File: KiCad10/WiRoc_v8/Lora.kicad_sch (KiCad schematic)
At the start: 16 parts, among them J1 TC2050, J11 Conn_01x05, J9 Conn_Coaxial, SW2 SW_SPST, U20 SY6280, U8 RAK3172-xx-43-SM-xI

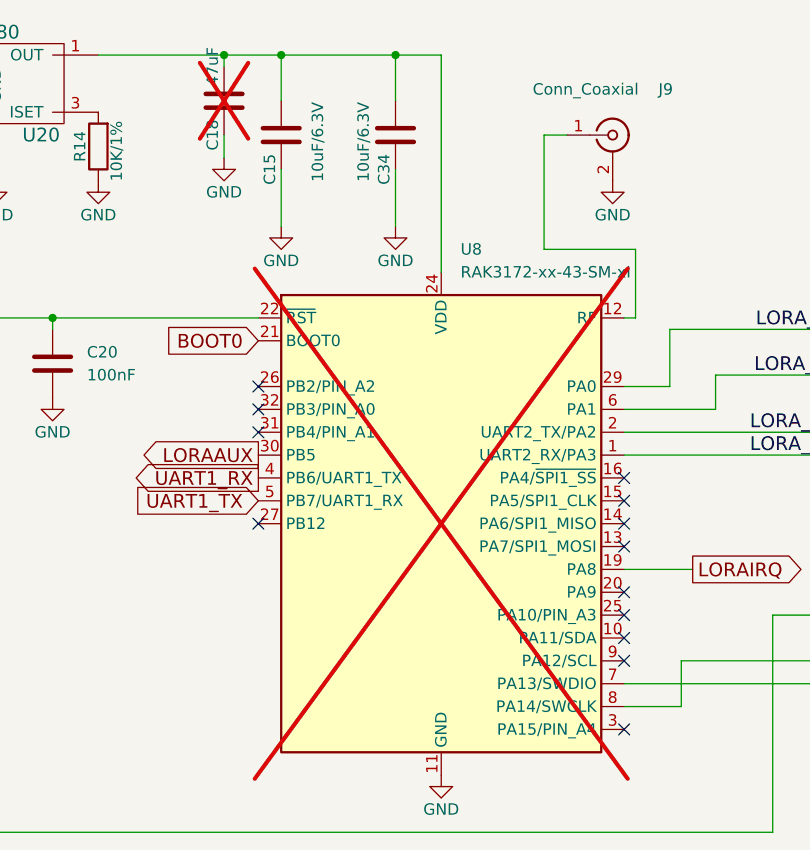
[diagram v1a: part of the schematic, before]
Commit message: add logo, improve layout
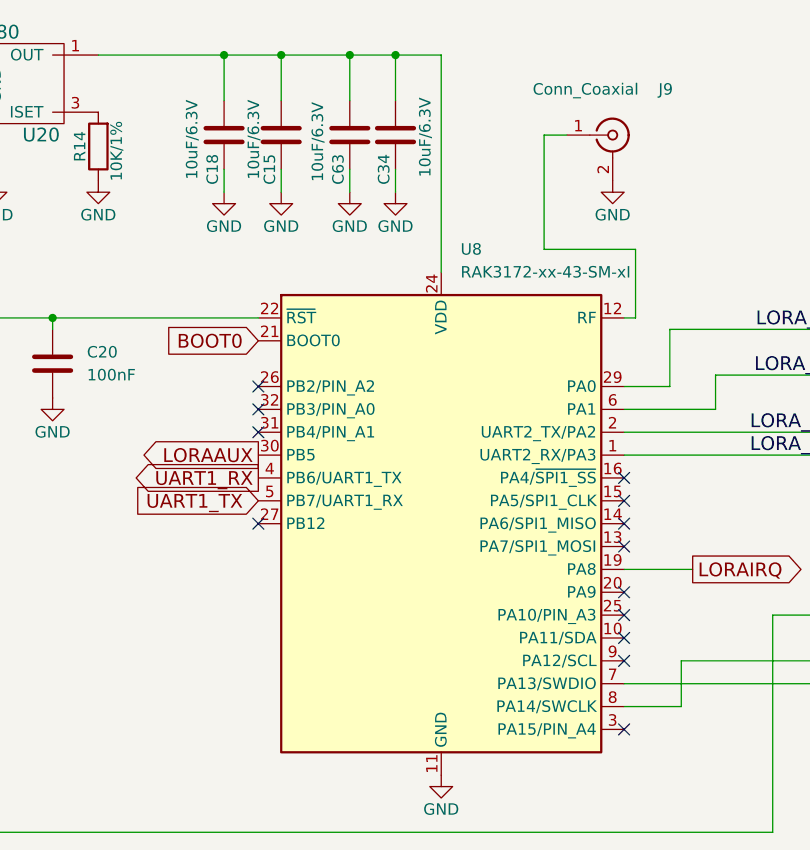
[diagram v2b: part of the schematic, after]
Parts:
- added C63: 10uF/6.3V, Capacitor_SMD:C_0402_1005Metric, symbol Device:C
- C18: value 47uF -> 10uF/6.3V; footprint Capacitor_SMD:C_1206_3216Metric -> Capacitor_SMD:C_0402_1005Metric; IncludeInBOM FALSE -> TRUE; LCSC Part # C96123 -> C15525; Manufacturer Murata Electronics -> Samsung Electro-Mechanics; ManufacturerPartNumber CL31A476MPHNNNE -> CL05A106MQ5NUNC; Package 1206 -> 0402; now fitted; now in the parts list
- U8: now fitted
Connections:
- net GND: now also C63.2
- net at C15.1, C18.1, C34.1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: now also C63.1

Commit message: etc
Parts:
- SW2: now left out of the parts list
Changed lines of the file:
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@@
 		(in_bom no)
 		(on_board yes)
-		(in_pos_files yes)
+		(in_pos_files no)
 		(dnp no)
 		(fields_autoplaced yes)
@@
 		(body_style 1)
 		(exclude_from_sim no)
-		(in_bom yes)
+		(in_bom no)
 		(on_board yes)
-		(in_pos_files yes)
+		(in_pos_files no)
 		(dnp no)
 		(fields_autoplaced yes)
@@
 		(in_bom no)
 		(on_board yes)
-		(in_pos_files yes)
+		(in_pos_files no)
 		(dnp no)
 		(fields_autoplaced yes)
@@
 		(in_bom no)
 		(on_board yes)
-		(in_pos_files yes)
+		(in_pos_files no)
 		(dnp no)
 		(fields_autoplaced yes)
